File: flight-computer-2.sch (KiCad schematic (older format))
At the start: 79 parts, among them J1 USB4105-GF-A, J2 THR, J3 SER1, J4 SER2, J5 SER3, J6 SER4, J7 Breakout L, J8 Breakout R, SW1 RESET, SW2 BOOT, U1 AP2114H-3.3TRG1, U2 MUN5214DW1T1G, U3 BNO080, U4 CP2102N, U5 MPL3115A2, U6 ESP32-PICO-D4, Y1 32.768kHz

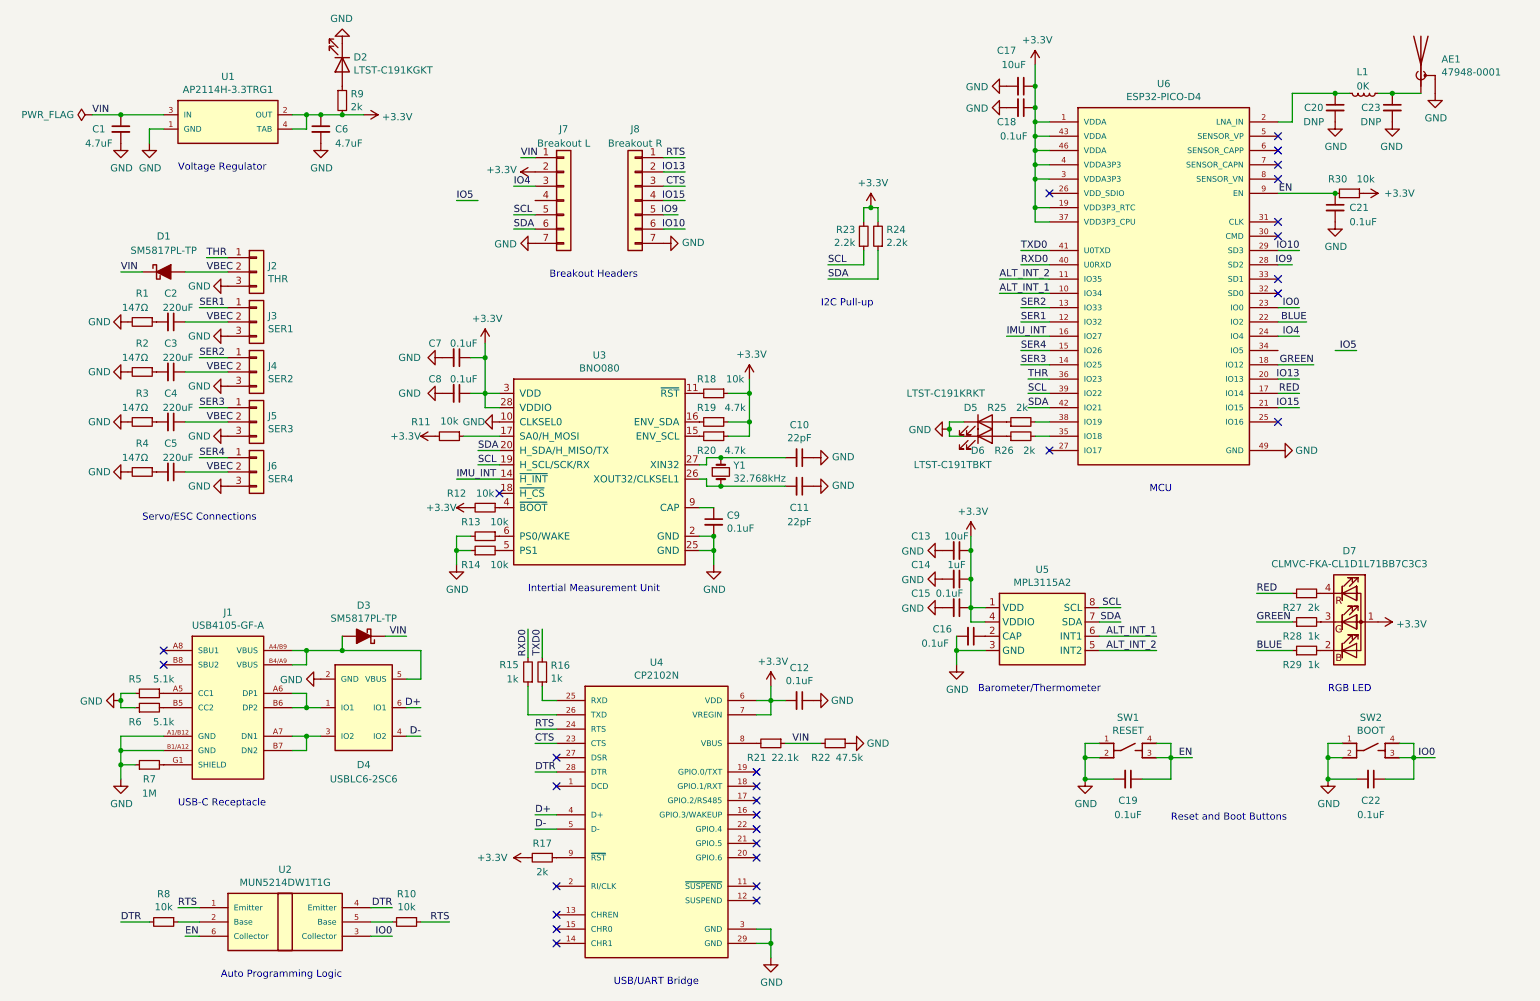
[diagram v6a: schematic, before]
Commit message: MOSFET to detect external power
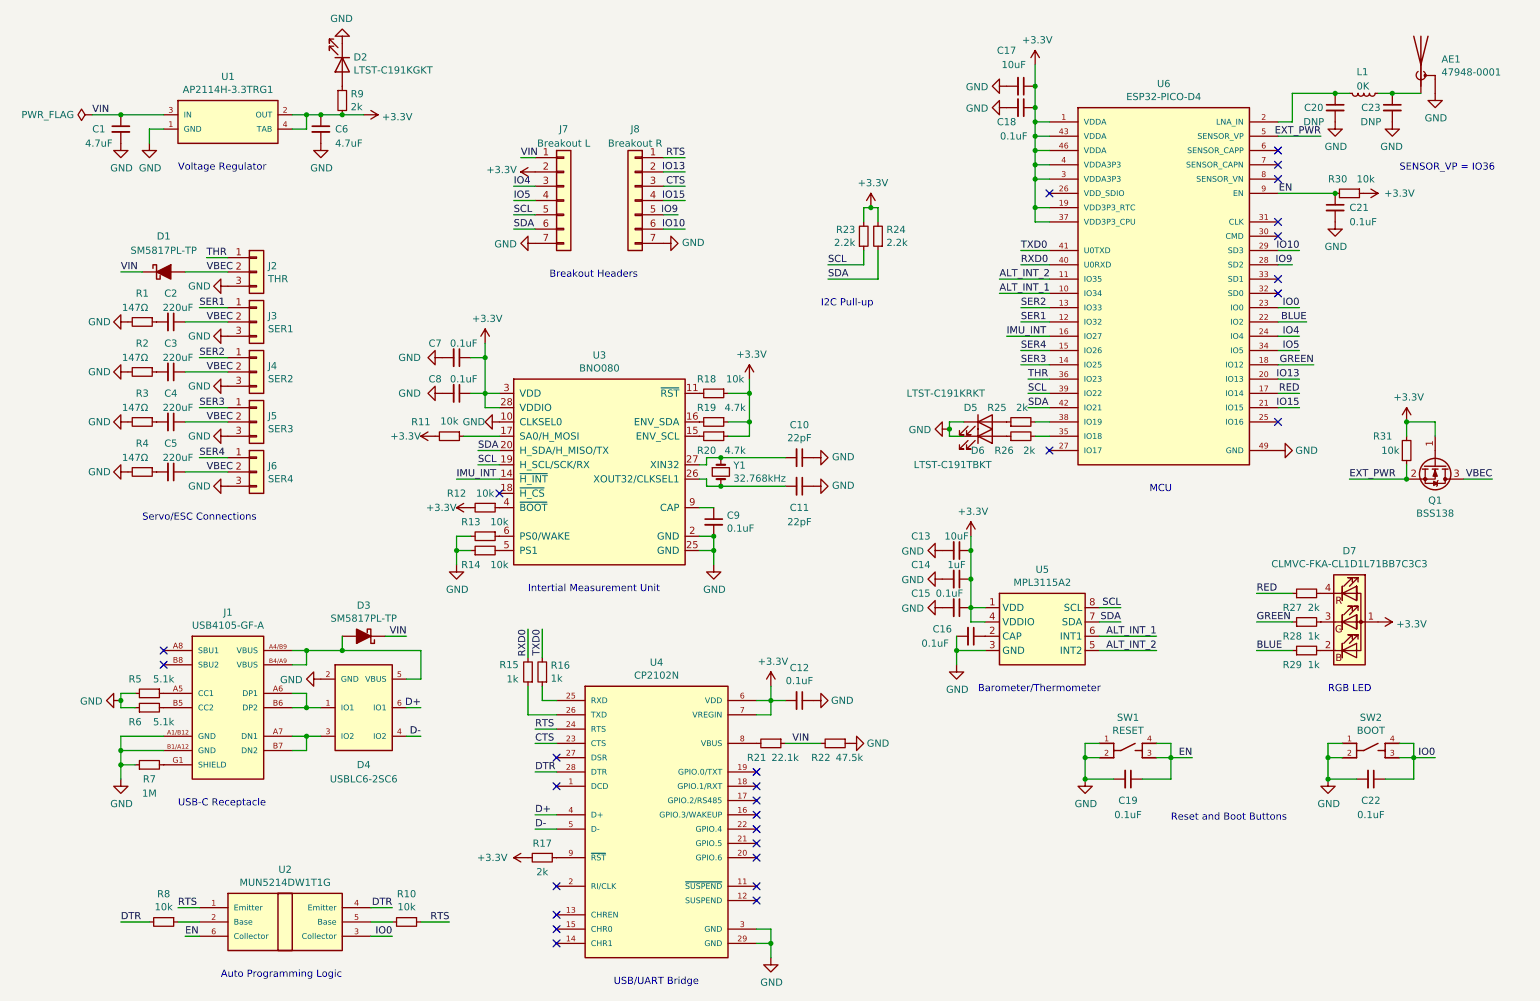
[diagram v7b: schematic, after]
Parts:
- added Q1: BSS138, flight-computer-2:SOT-23, symbol flight-computer-2:BSS138
- added R31: 10k, symbol Device:R_Small
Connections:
- net +3V3: now also Q1.1 (G), R31.2
- net IO5: now also J7.4 (Pin_4), U6.34 (IO5)
- net VBEC: now also Q1.3 (D)
- net EXT_PWR: now reaches U6.5 (SENSOR_VP)
- net EXT_PWR: now also Q1.2 (S), R31.1
- no-connect marks 29 -> 28
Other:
- note added: "SENSOR_VP = IO36"
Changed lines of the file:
@@
 Wire Wire Line
 	7800 3450 7650 3450
-NoConn ~ 9400 1550
 NoConn ~ 9400 1650
 NoConn ~ 9400 1750
@@
 Text Label 9550 2950 2    50   ~ 0
 IO4
-Text Label 9950 3050 2    50   ~ 0
+Text Label 9550 3050 2    50   ~ 0
 IO5
 Wire Wire Line
 	9400 2950 9550 2950
 Wire Wire Line
-	9800 3050 9950 3050
+	9400 3050 9550 3050
 Text Label 4050 1900 0    50   ~ 0
 IO4
-Text Label 3650 2000 0    50   ~ 0
+Text Label 4050 2000 0    50   ~ 0
 IO5
 Wire Wire Line
-	3650 2000 3800 2000
+	4050 2000 4200 2000
 Wire Wire Line
 	4050 1900 4200 1900
@@
 	9500 1250 9800 1250
 $Comp
-L power:GND #PWR055
+L power:GND #PWR056
 U 1 1 5F7B4947
 P 10500 1250
-F 0 "#PWR055" H 10500 1000 50  0001 C CNN
+F 0 "#PWR056" H 10500 1000 50  0001 C CNN
 F 1 "GND" H 10505 1077 50  0000 C CNN
 F 2 "" H 10500 1250 50  0001 C CNN
@@
 Text Label 1300 2500 0    50   ~ 0
 VIN
+$Comp
+L flight-computer-2:BSS138 Q1
+U 1 1 5F97A33A
+P 10500 3850
+F 0 "Q1" V 10749 3850 50  0000 C CNN
+F 1 "BSS138" V 10840 3850 50  0000 C CNN
+F 2 "flight-computer-2:SOT-23" H 10700 3775 50  0001 L CIN
+F 3 "~" H 10500 3850 50  0001 L CNN
+	1    10500 3850
+	0    1    1    0
+$EndComp
+Text Notes 10250 1800 0    50   ~ 0
+SENSOR_VP = IO36
+Text Label 9700 1550 2    50   ~ 0
+EXT_PWR
+Wire Wire Line
+	9700 1550 9400 1550
+$Comp
+L Device:R_Small R31
+U 1 1 5F9E3686
+P 10300 3750
+F 0 "R31" H 10200 3650 50  0000 R CNN
+F 1 "10k" H 10250 3750 50  0000 R CNN
+F 2 "" H 10300 3750 50  0001 C CNN
+F 3 "~" H 10300 3750 50  0001 C CNN
+	1    10300 3750
+	1    0    0    1
+$EndComp
+$Comp
+L power:+3.3V #PWR055
+U 1 1 5FA07E78
+P 10300 3550
+F 0 "#PWR055" H 10300 3400 50  0001 C CNN
+F 1 "+3.3V" H 10315 3723 50  0000 C CNN
+F 2 "" H 10300 3550 50  0001 C CNN
+F 3 "" H 10300 3550 50  0001 C CNN
+	1    10300 3550
+	1    0    0    -1
+$EndComp
+Text Label 10900 3950 2    50   ~ 0
+VBEC
+Wire Wire Line
+	10900 3950 10700 3950
+Text Label 9900 3950 0    50   ~ 0
+EXT_PWR
+Wire Wire Line
+	9900 3950 10300 3950
+Wire Wire Line
+	10300 3550 10300 3650
+Wire Wire Line
+	10300 3850 10300 3950
+Connection ~ 10300 3950
+Wire Wire Line
+	10500 3650 10500 3550
+Wire Wire Line
+	10500 3550 10300 3550
+Connection ~ 10300 3550
 $EndSCHEMATC

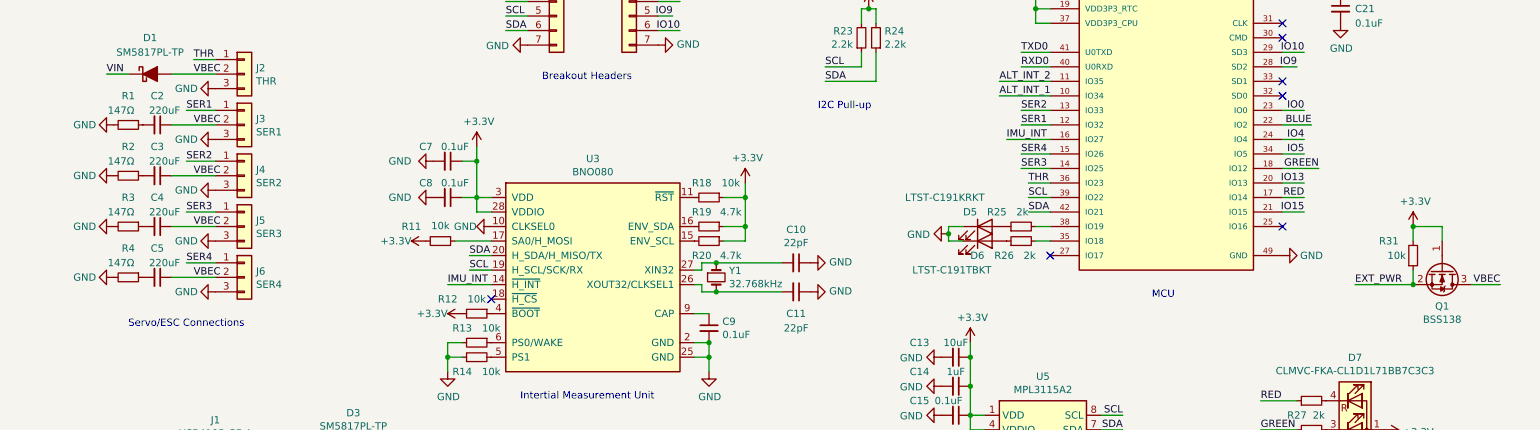
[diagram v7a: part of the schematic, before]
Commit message: Voltage divider and updated servo inrush resistors
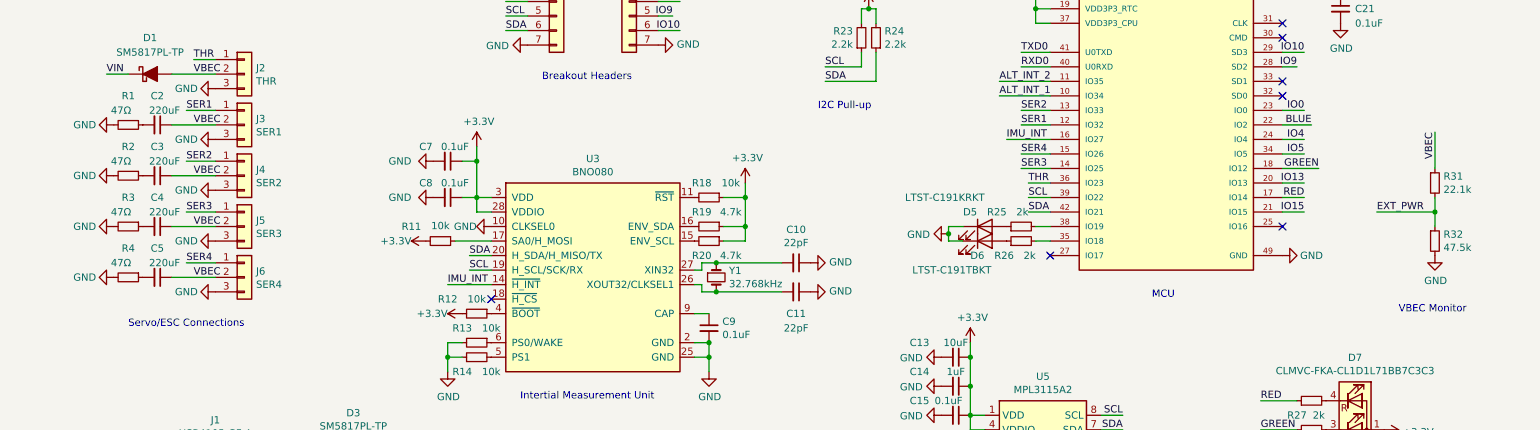
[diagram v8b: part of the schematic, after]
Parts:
- removed Q1: BSS138, flight-computer-2:SOT-23, symbol flight-computer-2:BSS138
- added R32: 47.5k, flight-computer-2:R_0603_1608Metric, symbol Device:R_Small
- C2, C3, C4, C5: footprint flight-computer-2:C_0603_1608Metric -> flight-computer-2:C_1206_3216Metric
- D1, D3: footprint flight-computer-2:D_PowerDI-5 -> flight-computer-2:D_SOD-123F
- R1, R2, R3, R4: value 147Ω -> 47Ω; footprint flight-computer-2:R_0603_1608Metric -> flight-computer-2:R_1206_3216Metric; MPN (none) -> ERJ-P08J470V
- R31: value 10k -> 22.1k; footprint (none) -> flight-computer-2:R_0603_1608Metric
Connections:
- net +3V3: no longer R31.2
- net EXT_PWR: now also R31.2, R32.1; no longer R31.1
- net GND: now also R32.2
- net VBEC: now also R31.1
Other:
- note added: "VBEC Monitor"
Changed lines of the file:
@@
 Sheet 1 1
 Title "VTOL EDF Flight Computer"
-Date "2020-07-28"
+Date "2020-07-29"
 Rev "v2"
 Comp ""
@@
 F 0 "D3" H 3000 4834 50  0000 C CNN
 F 1 "SM5817PL-TP" H 3000 4925 50  0000 C CNN
-F 2 "flight-computer-2:D_PowerDI-5" H 3000 5050 50  0001 C CNN
+F 2 "flight-computer-2:D_SOD-123F" H 3000 5050 50  0001 C CNN
 F 3 "~" H 3000 5050 50  0001 C CNN
 F 4 "PDS4150-13" H 3000 5050 50  0001 C CNN "MPN"
@@
 F 0 "D1" H 1600 2750 50  0000 C CNN
 F 1 "SM5817PL-TP" H 1600 2650 50  0000 C CNN
-F 2 "flight-computer-2:D_PowerDI-5" H 1600 2500 50  0001 C CNN
+F 2 "flight-computer-2:D_SOD-123F" H 1600 2500 50  0001 C CNN
 F 3 "~" H 1600 2500 50  0001 C CNN
 F 4 "PDS4150-13" H 1600 2500 50  0001 C CNN "MPN"
@@
 F 0 "C2" V 1450 2850 50  0000 C CNN
 F 1 "220uF" V 1550 2900 50  0000 C CNN
-F 2 "flight-computer-2:C_0603_1608Metric" H 1650 2850 50  0001 C CNN
+F 2 "flight-computer-2:C_1206_3216Metric" H 1650 2850 50  0001 C CNN
 F 3 "~" H 1650 2850 50  0001 C CNN
 F 4 "GRM31CR60J227ME11L" V 1650 2850 50  0001 C CNN "MPN"
@@
 P 1450 2850
 F 0 "R1" V 1250 2850 50  0000 C CNN
-F 1 "147Ω" V 1350 2800 50  0000 C CNN
-F 2 "flight-computer-2:R_0603_1608Metric" H 1450 2850 50  0001 C CNN
+F 1 "47Ω" V 1350 2800 50  0000 C CNN
+F 2 "flight-computer-2:R_1206_3216Metric" H 1450 2850 50  0001 C CNN
 F 3 "~" H 1450 2850 50  0001 C CNN
+F 4 "ERJ-P08J470V" V 1450 2850 50  0001 C CNN "MPN"
 	1    1450 2850
 	0    1    1    0
@@
 F 0 "C3" V 1450 3200 50  0000 C CNN
 F 1 "220uF" V 1550 3250 50  0000 C CNN
-F 2 "flight-computer-2:C_0603_1608Metric" H 1650 3200 50  0001 C CNN
+F 2 "flight-computer-2:C_1206_3216Metric" H 1650 3200 50  0001 C CNN
 F 3 "~" H 1650 3200 50  0001 C CNN
 F 4 "GRM31CR60J227ME11L" V 1650 3200 50  0001 C CNN "MPN"
@@
 F 0 "C4" V 1450 3550 50  0000 C CNN
 F 1 "220uF" V 1550 3600 50  0000 C CNN
-F 2 "flight-computer-2:C_0603_1608Metric" H 1650 3550 50  0001 C CNN
+F 2 "flight-computer-2:C_1206_3216Metric" H 1650 3550 50  0001 C CNN
 F 3 "~" H 1650 3550 50  0001 C CNN
 F 4 "GRM31CR60J227ME11L" V 1650 3550 50  0001 C CNN "MPN"
@@
 F 0 "C5" V 1450 3900 50  0000 C CNN
 F 1 "220uF" V 1550 3950 50  0000 C CNN
-F 2 "flight-computer-2:C_0603_1608Metric" H 1650 3900 50  0001 C CNN
+F 2 "flight-computer-2:C_1206_3216Metric" H 1650 3900 50  0001 C CNN
 F 3 "~" H 1650 3900 50  0001 C CNN
 F 4 "GRM31CR60J227ME11L" V 1650 3900 50  0001 C CNN "MPN"
@@
 P 1450 3200
 F 0 "R2" V 1250 3200 50  0000 C CNN
-F 1 "147Ω" V 1350 3150 50  0000 C CNN
-F 2 "flight-computer-2:R_0603_1608Metric" H 1450 3200 50  0001 C CNN
+F 1 "47Ω" V 1350 3150 50  0000 C CNN
+F 2 "flight-computer-2:R_1206_3216Metric" H 1450 3200 50  0001 C CNN
 F 3 "~" H 1450 3200 50  0001 C CNN
+F 4 "ERJ-P08J470V" V 1450 3200 50  0001 C CNN "MPN"
 	1    1450 3200
 	0    1    1    0
@@
 P 1450 3550
 F 0 "R3" V 1250 3550 50  0000 C CNN
-F 1 "147Ω" V 1350 3500 50  0000 C CNN
-F 2 "flight-computer-2:R_0603_1608Metric" H 1450 3550 50  0001 C CNN
+F 1 "47Ω" V 1350 3500 50  0000 C CNN
+F 2 "flight-computer-2:R_1206_3216Metric" H 1450 3550 50  0001 C CNN
 F 3 "~" H 1450 3550 50  0001 C CNN
+F 4 "ERJ-P08J470V" V 1450 3550 50  0001 C CNN "MPN"
 	1    1450 3550
 	0    1    1    0
@@
 P 1450 3900
 F 0 "R4" V 1250 3900 50  0000 C CNN
-F 1 "147Ω" V 1350 3850 50  0000 C CNN
-F 2 "flight-computer-2:R_0603_1608Metric" H 1450 3900 50  0001 C CNN
+F 1 "47Ω" V 1350 3850 50  0000 C CNN
+F 2 "flight-computer-2:R_1206_3216Metric" H 1450 3900 50  0001 C CNN
 F 3 "~" H 1450 3900 50  0001 C CNN
+F 4 "ERJ-P08J470V" V 1450 3900 50  0001 C CNN "MPN"
 	1    1450 3900
 	0    1    1    0
@@
 Text Label 1300 2500 0    50   ~ 0
 VIN
-$Comp
-L flight-computer-2:BSS138 Q1
-U 1 1 5F97A33A
-P 10500 3850
-F 0 "Q1" V 10749 3850 50  0000 C CNN
-F 1 "BSS138" V 10840 3850 50  0000 C CNN
-F 2 "flight-computer-2:SOT-23" H 10700 3775 50  0001 L CIN
-F 3 "~" H 10500 3850 50  0001 L CNN
-	1    10500 3850
-	0    1    1    0
-$EndComp
 Text Notes 10250 1800 0    50   ~ 0
 SENSOR_VP = IO36
@@
 Wire Wire Line
 	9700 1550 9400 1550
+Text Label 10450 2900 3    50   ~ 0
+VBEC
+Text Label 10050 3450 0    50   ~ 0
+EXT_PWR
+Wire Wire Line
+	10050 3450 10450 3450
+Wire Wire Line
+	10450 3150 10450 2900
 $Comp
 L Device:R_Small R31
-U 1 1 5F9E3686
-P 10300 3750
-F 0 "R31" H 10200 3650 50  0000 R CNN
-F 1 "10k" H 10250 3750 50  0000 R CNN
-F 2 "" H 10300 3750 50  0001 C CNN
-F 3 "~" H 10300 3750 50  0001 C CNN
-	1    10300 3750
-	1    0    0    1
-$EndComp
-$Comp
-L power:+3.3V #PWR055
-U 1 1 5FA07E78
-P 10300 3550
-F 0 "#PWR055" H 10300 3400 50  0001 C CNN
-F 1 "+3.3V" H 10315 3723 50  0000 C CNN
-F 2 "" H 10300 3550 50  0001 C CNN
-F 3 "" H 10300 3550 50  0001 C CNN
-	1    10300 3550
-	1    0    0    -1
-$EndComp
-Text Label 10900 3950 2    50   ~ 0
-VBEC
-Wire Wire Line
-	10900 3950 10700 3950
-Text Label 9900 3950 0    50   ~ 0
-EXT_PWR
-Wire Wire Line
-	9900 3950 10300 3950
-Wire Wire Line
-	10300 3550 10300 3650
-Wire Wire Line
-	10300 3850 10300 3950
-Connection ~ 10300 3950
-Wire Wire Line
-	10500 3650 10500 3550
-Wire Wire Line
-	10500 3550 10300 3550
-Connection ~ 10300 3550
+U 1 1 5FBFFDBC
+P 10450 3250
+F 0 "R31" H 10509 3296 50  0000 L CNN
+F 1 "22.1k" H 10509 3205 50  0000 L CNN
+F 2 "flight-computer-2:R_0603_1608Metric" H 10450 3250 50  0001 C CNN
+F 3 "~" H 10450 3250 50  0001 C CNN
+	1    10450 3250
+	1    0    0    -1
+$EndComp
+$Comp
+L Device:R_Small R32
+U 1 1 5FC107AE
+P 10450 3650
+F 0 "R32" H 10509 3696 50  0000 L CNN
+F 1 "47.5k" H 10509 3605 50  0000 L CNN
+F 2 "flight-computer-2:R_0603_1608Metric" H 10450 3650 50  0001 C CNN
+F 3 "~" H 10450 3650 50  0001 C CNN
+	1    10450 3650
+	1    0    0    -1
+$EndComp
+$Comp
+L power:GND #PWR055
+U 1 1 5FC117FA
+P 10450 3750
+F 0 "#PWR055" H 10450 3500 50  0001 C CNN
+F 1 "GND" H 10455 3577 50  0000 C CNN
+F 2 "" H 10450 3750 50  0001 C CNN
+F 3 "" H 10450 3750 50  0001 C CNN
+	1    10450 3750
+	1    0    0    -1
+$EndComp
+Wire Wire Line
+	10450 3350 10450 3450
+Connection ~ 10450 3450
+Wire Wire Line
+	10450 3450 10450 3550
+Text Notes 10200 4150 0    50   ~ 0
+VBEC Monitor
 $EndSCHEMATC
